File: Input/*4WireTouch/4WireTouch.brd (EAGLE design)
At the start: 20 x 13 mm, 8 parts

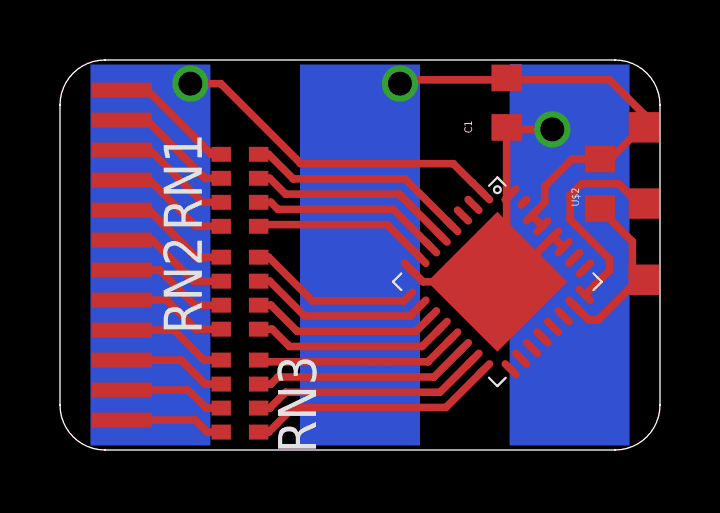
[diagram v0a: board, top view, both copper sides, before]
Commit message: Update Pinheader
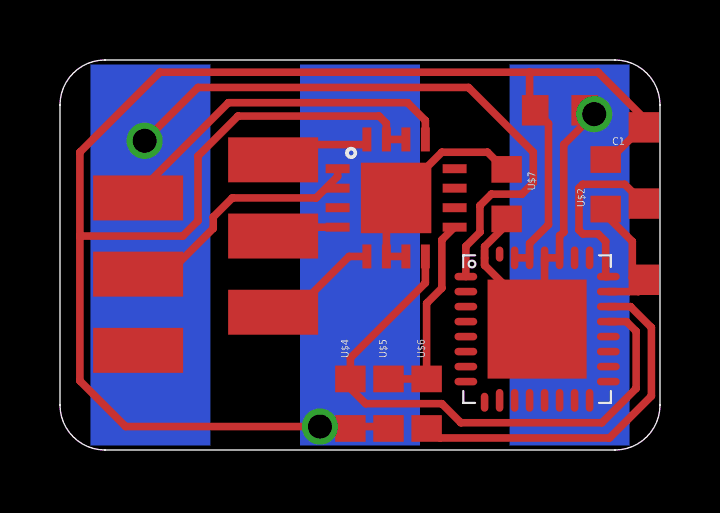
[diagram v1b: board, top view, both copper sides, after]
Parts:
- removed RN1, RN2, RN3: 68, resistor-dil:0603-ARC
- added U$12: PINHD_6MICROMATCH, thar:MICROMATCH6POL
- added U$3: AD7879, thar:LFCSP
- added U$4, U$5: 4.7k, thar:603
- added U$7: 0, thar:603
- U$6: value PINHD_12 -> 0; device thar:FFC12/1MM -> thar:603
- moved U$6 11.3 mm to (14.0, 2.79), turned to 270 degrees
- moved U$10 2.06 mm to (17.7, 5.28), turned to 0 degrees
- moved C1 1.80 mm to (18.4, 12.6), turned to 0 degrees
- moved U$2 0.19 mm to (19.9, 10.1)
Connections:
- removed net N$17: RN2.8, U$10.9
- removed net N$18: RN1.5, U$10.7
- removed net N$19: RN1.6, U$10.6
- removed net N$20: RN1.7, U$10.5
- removed net N$21: RN1.8, U$10.4
- removed net N$22: RN1.1, U$6.P$12
- removed net N$24: RN1.2, U$6.P$11
- removed net N$38: RN1.3, U$6.P$10
- removed net N$39: RN1.4, U$6.P$9
- removed net N$40: RN2.1, U$6.P$8
- removed net N$41: RN2.2, U$6.P$7
- removed net N$42: RN2.3, U$6.P$6
- removed net N$43: RN2.4, U$6.P$5
- removed net N$44: RN3.5, U$6.P$4
- removed net N$45: RN3.6, U$6.P$3
- removed net N$47: RN3.8, U$6.P$1
- new net N$15: U$10.22, U$6.2
- net GND: now also U$7.2; no longer U$10.8
- net N$11: now also U$12.P$4, U$3.P$4; no longer RN3.4, U$10.13
- net N$13: now also U$12.P$3, U$3.P$1; no longer RN2.5, U$10.12
- net N$14: now also U$12.P$6, U$3.P$16; no longer RN2.6, U$10.11
- net N$16: now also U$3.P$6, U$3.P$7, U$7.1; no longer RN2.7, U$10.10
- net N$2: now also U$10.21, U$3.P$8, U$4.1; no longer RN3.1, U$10.16
- net N$5: now also U$3.P$9, U$5.1, U$6.1; no longer RN3.7, U$6.P$2
- net N$6: now also U$12.P$5, U$3.P$13; no longer RN3.2, U$10.15
- net N$7: now also U$12.P$2, U$3.P$5; no longer RN3.3, U$10.14
- net VCC: now also U$3.P$14, U$3.P$15, U$4.2, U$5.2
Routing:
- net VCC: track 22.1 -> 79.4 mm
- net N$15: track 0.00 -> 12.2 mm
- net N$2: track 8.38 -> 19.0 mm
- net N$12: track 17.6 -> 25.7 mm
- net N$21: track 7.45 -> 0.00 mm
- net N$20: track 6.91 -> 0.00 mm
- net N$19: track 6.37 -> 0.00 mm
- net N$18: track 5.90 -> 0.00 mm
- net N$17: track 5.66 -> 0.00 mm
- net GND: track 22.8 -> 27.8 mm
- net N$11: track 6.84 -> 2.27 mm
- net N$22: track 4.20 -> 0.00 mm
- net N$24: track 4.12 -> 0.00 mm
- net N$38: track 4.03 -> 0.00 mm
- net N$6: track 7.84 -> 11.9 mm
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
